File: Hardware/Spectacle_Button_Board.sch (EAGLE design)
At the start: 40 parts, among them J19 FTDI_DEVICE, U1 CY8C4146LQI-S422, U2 MIC5205-5V

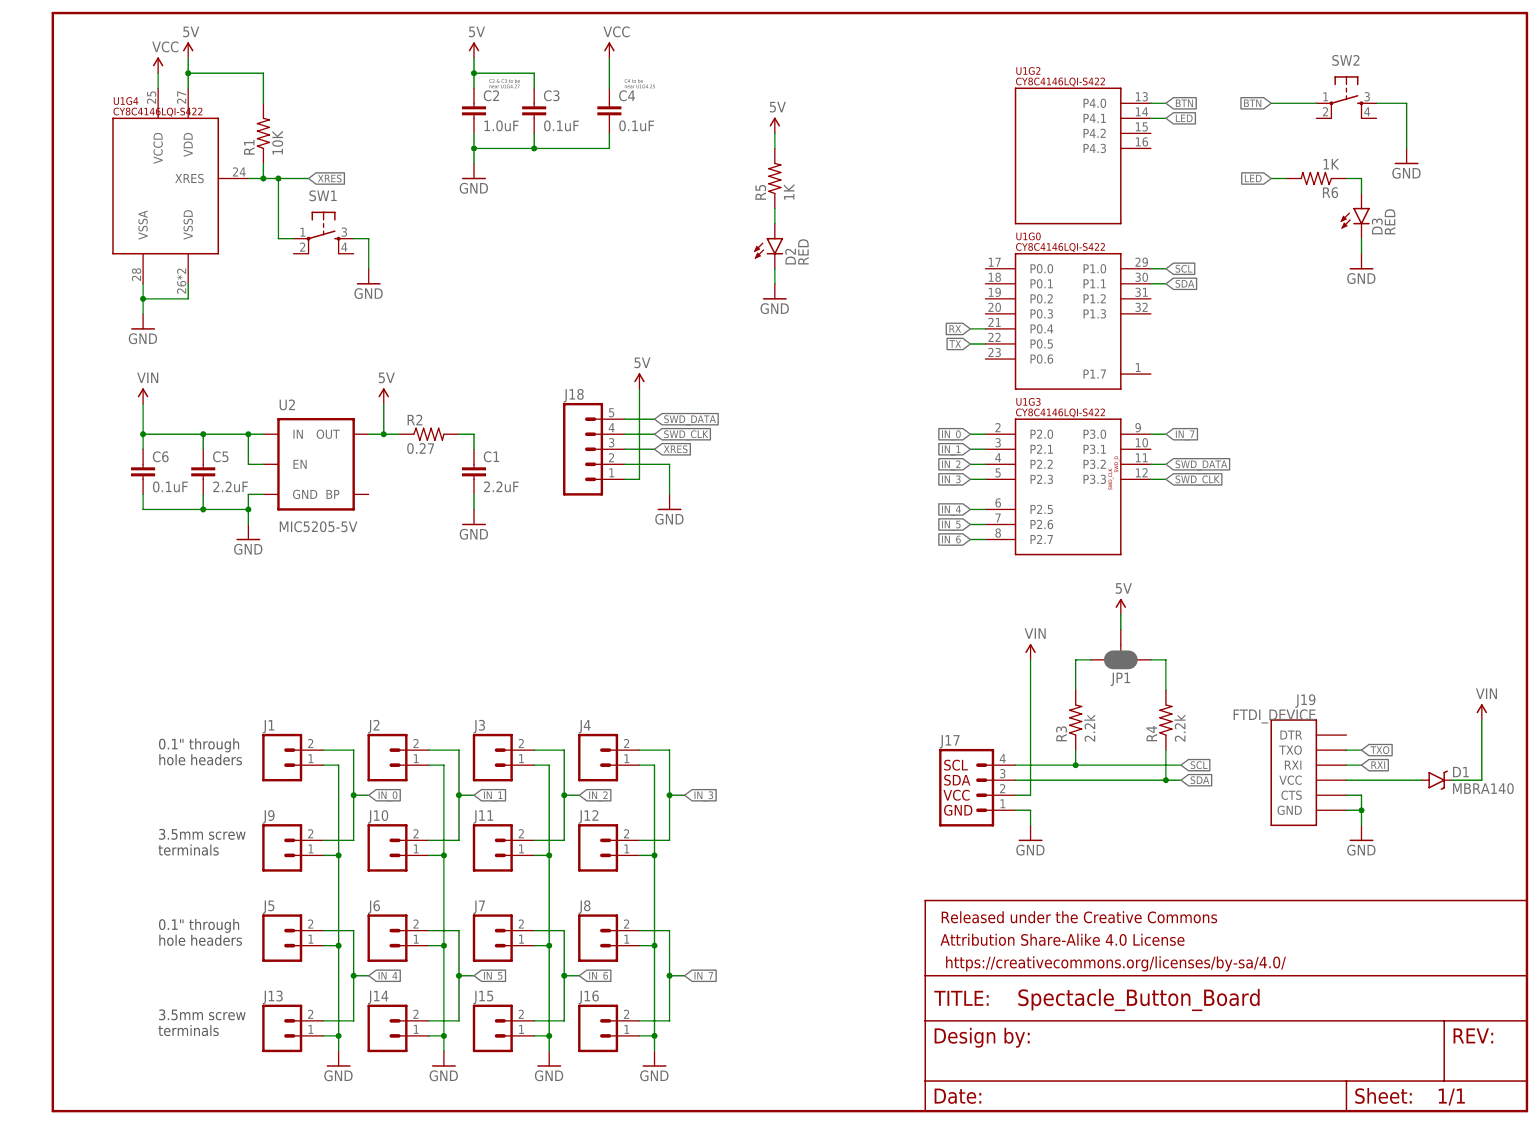
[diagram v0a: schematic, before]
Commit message: Make some chgs (see full msg) - Add TVS diodes to all button and data/power lines - Partition schematic according to function - Change power/data connector to TRRS
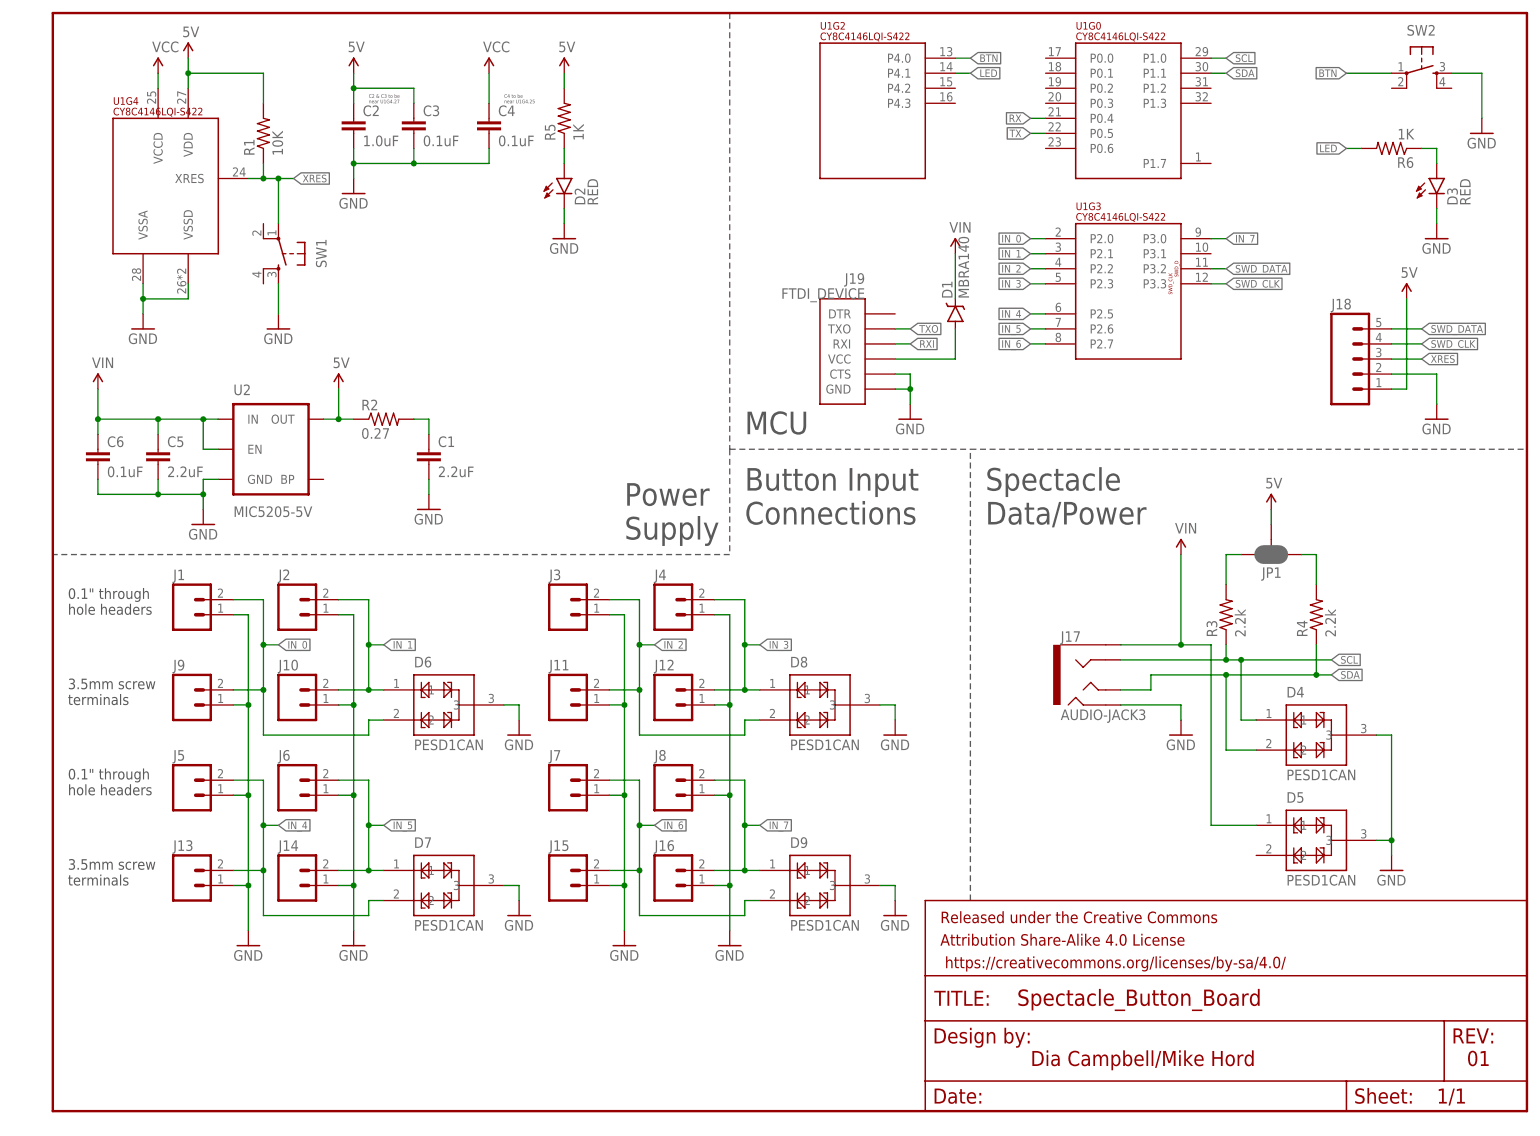
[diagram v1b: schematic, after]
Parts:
- added D4, D5, D6, D7, D8, D9: PESD1CAN, SparkFun-DiscreteSemi:PESD1CAN
- J17: value (none) -> AUDIO-JACK3; device SparkFun-Connectors:I2C_STANDARD -> SparkFun-Connectors:AUDIO-JACK3
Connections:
- net GND: now also D4.3, D5.3, D6.3, D7.3, D8.3, D9.3, J17.RING2; no longer J17.1
- net IN_0: now also D6.2
- net IN_1: now also D6.1
- net IN_2: now also D8.2
- net IN_3: now also D8.1
- net IN_4: now also D7.2
- net IN_5: now also D7.1
- net IN_6: now also D9.2
- net IN_7: now also D9.1
- net SCL: now also D4.1, J17.RING1; no longer J17.4
- net SDA: now also D4.2, J17.TIP; no longer J17.3
- net VIN: now also D5.1, J17.EARTH; no longer J17.2
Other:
- note added: "01"
- note added: "Button Input Connections"
- note added: "Dia Campbell/Mike Hord"
- note added: "MCU"
- note added: "Power Supply"
- note added: "Spectacle Data/Power"
- moved on the sheet: C1, C2, C3, C4, C5, C6, D1, D2, D3, J1, J10, J11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

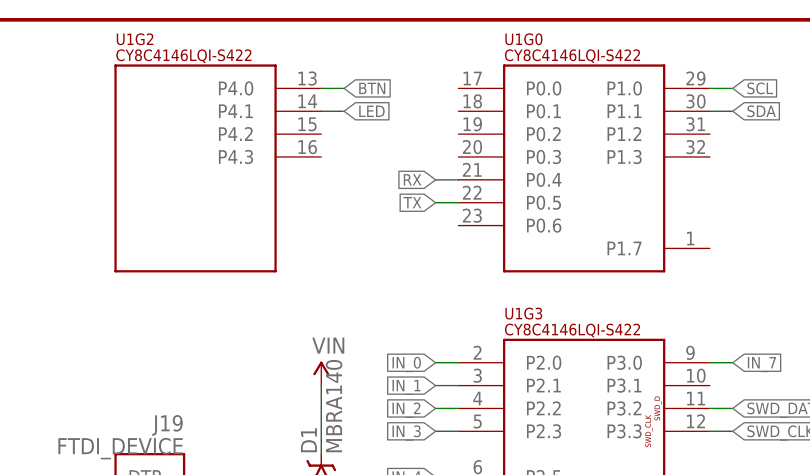
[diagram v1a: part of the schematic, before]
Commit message: Fix TX and RX net names
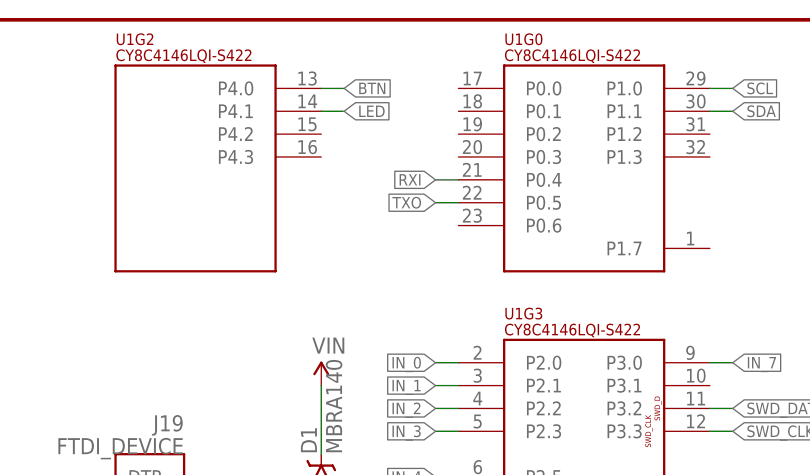
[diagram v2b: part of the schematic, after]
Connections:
- removed net RX: U1G0.P0.4
- removed net TX: U1G0.P0.5
- net RXI: now also U1G0.P0.4
- net TXO: now also U1G0.P0.5
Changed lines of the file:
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@@
 <label x="144.78" y="132.08" size="1.27" layer="95" xref="yes"/>
+</segment>
+<segment>
+<pinref part="U1" gate="G0" pin="P0.5"/>
+<wire x1="167.64" y1="165.1" x2="165.1" y2="165.1" width="0.1524" layer="91"/>
+<label x="165.1" y="165.1" size="1.27" layer="95" rot="R180" xref="yes"/>
 </segment>
 </net>
@@
 <label x="144.78" y="129.54" size="1.27" layer="95" xref="yes"/>
 </segment>
-</net>
-<net name="RX" class="0">
 <segment>
 <pinref part="U1" gate="G0" pin="P0.4"/>
@@
 </segment>
 </net>
-<net name="TX" class="0">
-<segment>
-<pinref part="U1" gate="G0" pin="P0.5"/>
-<wire x1="167.64" y1="165.1" x2="165.1" y2="165.1" width="0.1524" layer="91"/>
-<label x="165.1" y="165.1" size="1.27" layer="95" rot="R180" xref="yes"/>
-</segment>
-</net>
